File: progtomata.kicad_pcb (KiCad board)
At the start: 2 copper layers, 28 parts, among them J1 Conn_01x04_Pin, J2 Conn_01x04_Pin, P1 USB_C_Plug_USB2.0, SW1 SW_SPDT, U1 STM32F407VGTx, U2 AMS1117-3.3, Y1 8MHz

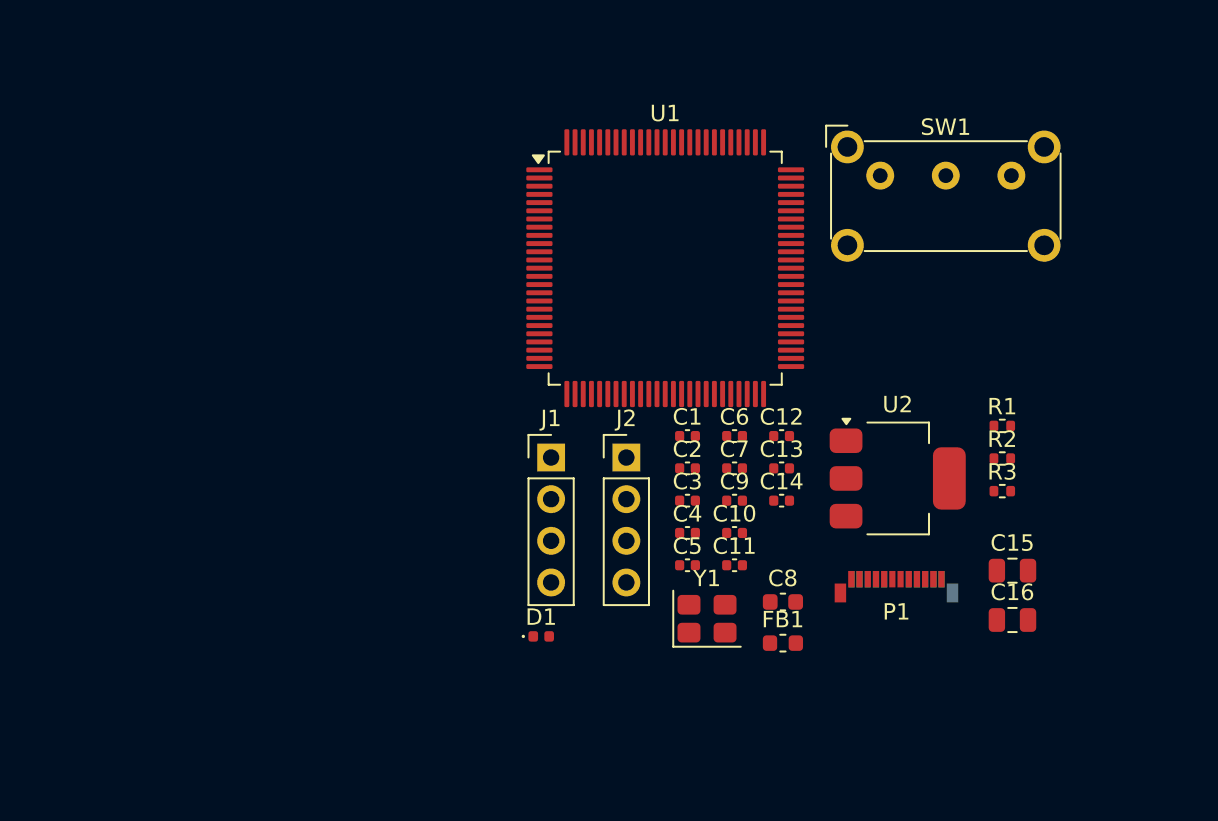
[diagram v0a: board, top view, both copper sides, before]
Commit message: Add 8-bit priority encoder
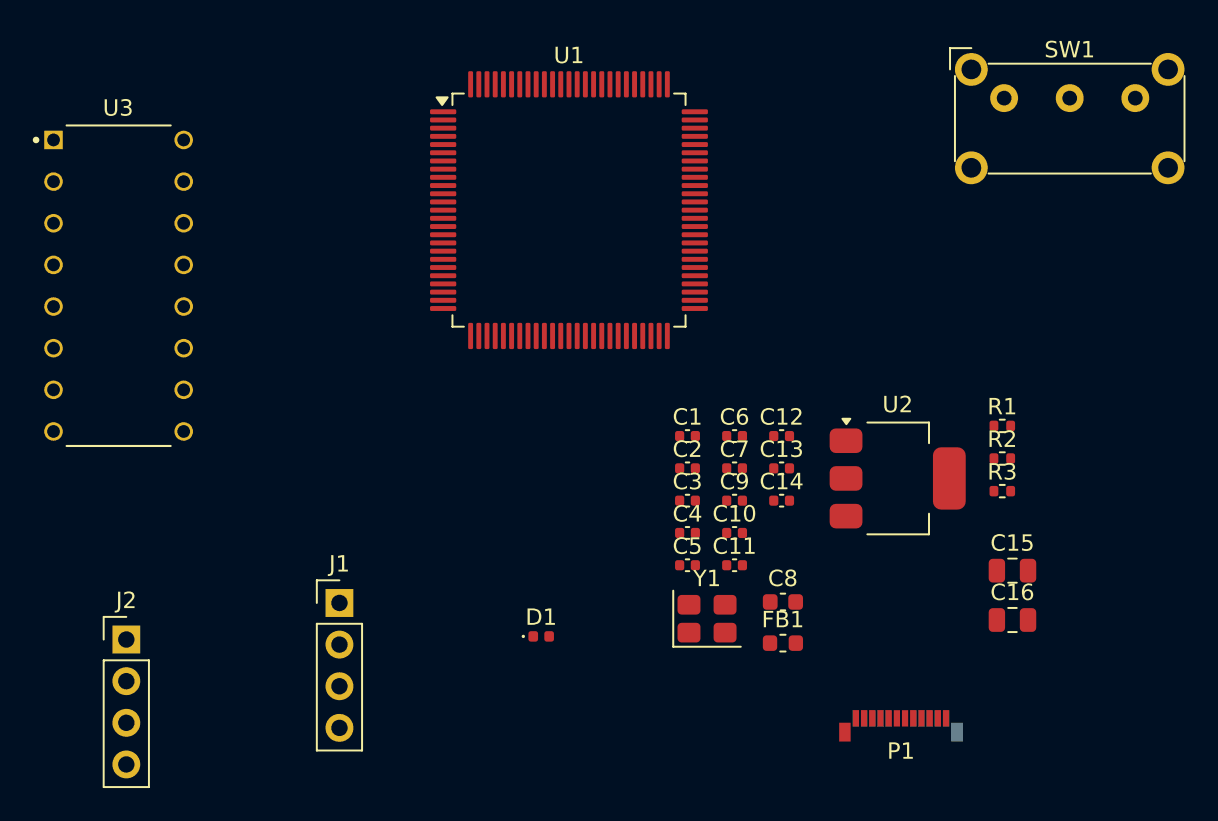
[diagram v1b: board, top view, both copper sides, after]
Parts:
- added U3: CD4532BE, CD4532BE:DIP794W45P254L1969H508Q16, F.Cu at (106.5, 79.1)
- moved J2 32.5 mm to (107.0, 100.7)
- moved J1 15.7 mm to (120.0, 98.5)
- moved SW1 8.91 mm to (160.5, 67.7)
- moved P1 8.49 mm to (154.2, 105.5)
- moved U1 6.85 mm to (134.0, 74.5)
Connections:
- U1 pad 67: unconnected-(U1-PA8-Pad67) -> ENC1_Q0
- U1 pad 68: unconnected-(U1-PA9-Pad68) -> ENC1_Q1
- U1 pad 77: unconnected-(U1-PA15-Pad77) -> ENC1_Q2

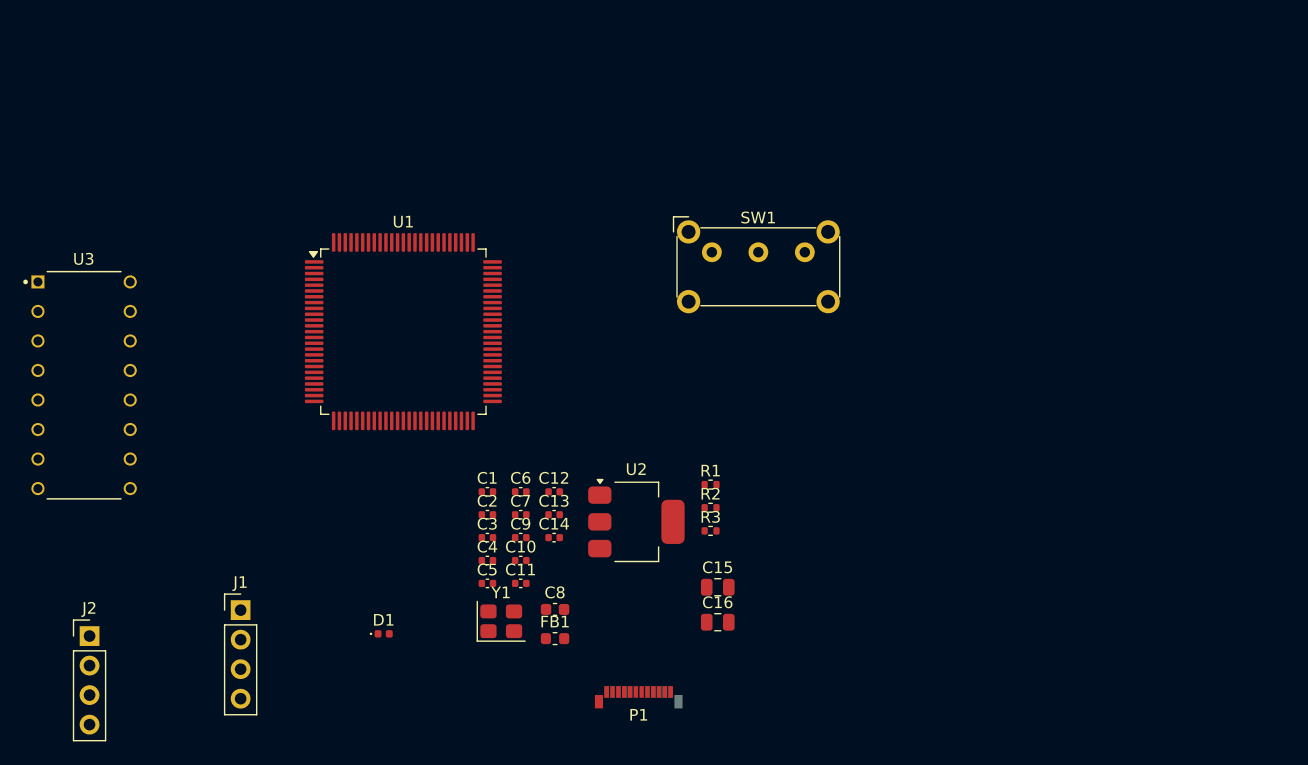
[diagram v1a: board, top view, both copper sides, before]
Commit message: Change priority encoder footprint
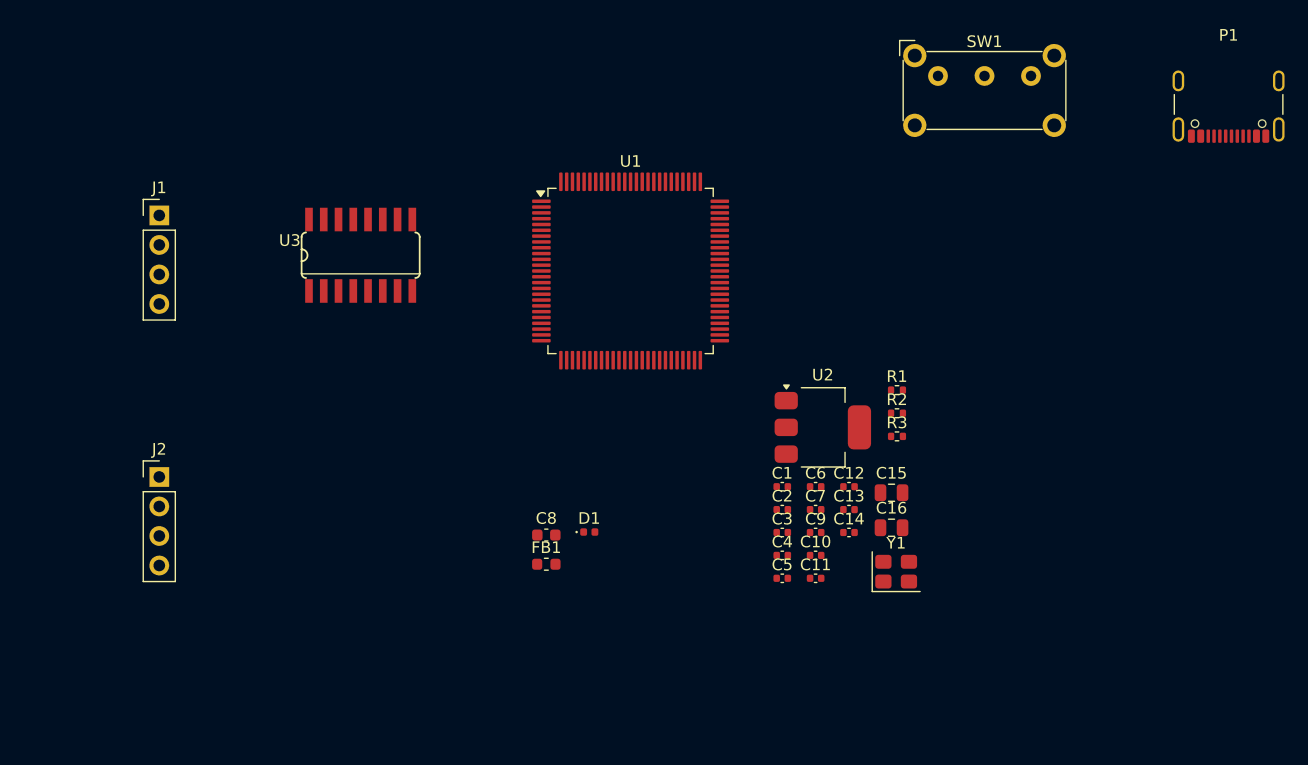
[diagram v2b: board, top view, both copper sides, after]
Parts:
- P1: footprint Connector_USB:USB_C_Plug_Molex_105444 -> Connector_USB:USB_C_Receptacle_GCT_USB4105-xx-A_16P_TopMnt_Horizontal
- U3: value CD4532BE -> 74LS148; footprint CD4532BE:DIP794W45P254L1969H508Q16 -> 74148:SO16
- moved P1 72.3 mm to (205.0, 54.0), turned to 180 degrees
- moved J1 34.7 mm to (113.0, 64.5)
- moved Y1 34.2 mm to (176.4, 95.2)
- moved U3 26.3 mm to (130.3, 67.9)
- moved C1 25.4 mm to (166.6, 87.8)
- moved C10 25.4 mm to (169.5, 93.8)
- moved C11 25.4 mm to (169.5, 95.7)
- moved C12 25.4 mm to (172.3, 87.8)
- moved C13 25.4 mm to (172.3, 89.8)
- moved C14 25.4 mm to (172.3, 91.8)
- moved C2 25.4 mm to (166.6, 89.8)
- moved C3 25.4 mm to (166.6, 91.8)
- moved C4 25.4 mm to (166.6, 93.8)
- moved C5 25.4 mm to (166.6, 95.7)
- moved C6 25.4 mm to (169.5, 87.8)
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
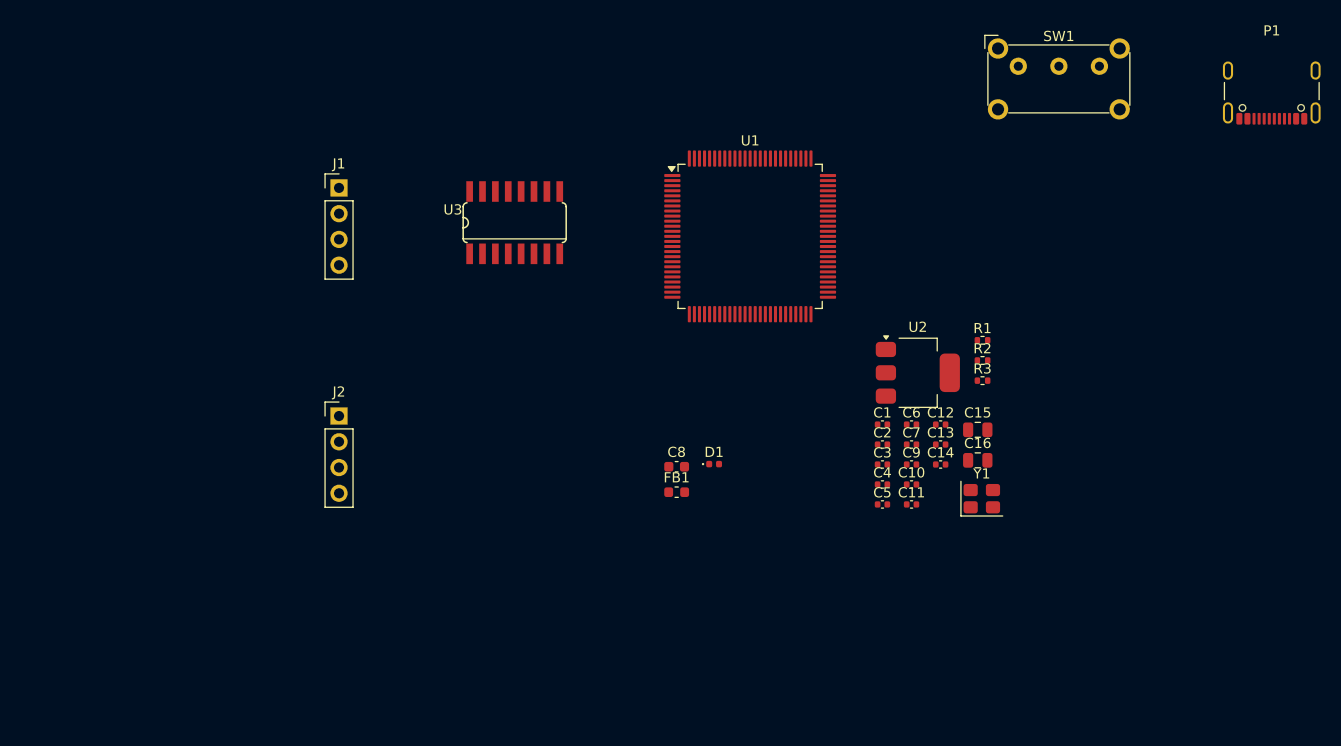
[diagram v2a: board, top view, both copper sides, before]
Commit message: Update PCB footprint (USB-C port, button priority encoder)
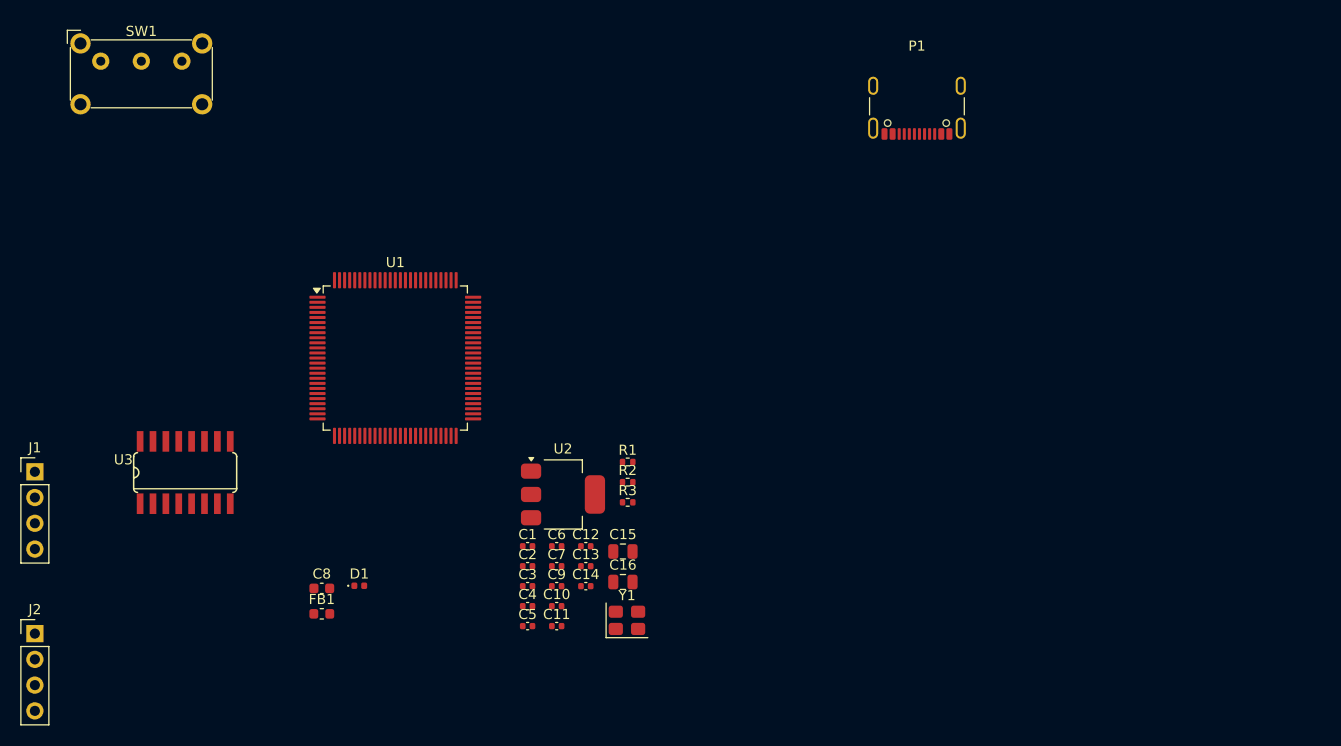
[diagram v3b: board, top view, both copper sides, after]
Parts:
- U3: footprint 74148:SO16 -> 74LS148:SO16
- moved SW1 90.5 mm to (89.5, 52.0)
- moved J1 41.0 mm to (83.0, 92.5)
- moved U3 40.8 mm to (97.8, 92.6)
- moved C8 37.0 mm to (111.3, 104.0)
- moved FB1 37.0 mm to (111.3, 106.5)
- moved U1 37.0 mm to (118.5, 81.3)
- moved C1 37.0 mm to (131.6, 99.8)
- moved C10 37.0 mm to (134.5, 105.8)
- moved C11 37.0 mm to (134.5, 107.7)
- moved C12 37.0 mm to (137.3, 99.8)
- moved C13 37.0 mm to (137.3, 101.8)
- moved C14 37.0 mm to (137.3, 103.8)
- moved C15 37.0 mm to (141.0, 100.4)
- moved C16 37.0 mm to (141.0, 103.4)
- moved C2 37.0 mm to (131.6, 101.8)
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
